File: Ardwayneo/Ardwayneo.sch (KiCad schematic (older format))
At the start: 13 parts, among them U1 24LC1025, U2 24LC1025, U3 ATMEGA328P-AU, Y1 Crystal 32MHz, Y2 Crystal 16MHz

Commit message: Completed all wiring
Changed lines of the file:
@@
 F16 "D7" B R 5875 6300 50
 F17 "D8" B R 5875 6450 50
+F18 "I2C" B R 5875 5275 50
 $EndSheet
 $Comp
@@
 Wire Wire Line
 	3900 5075 4125 5075
-Text Label 7250 3100 2    50   ~ 0
+Text Label 7450 3100 2    50   ~ 0
 MISO
-Wire Wire Line
-	7250 3100 7450 3100
 Text Label 3900 5300 2    50   ~ 0
 SCK
@@
 Text Label 3900 6625 2    50   ~ 0
 GND
-Text Label 7250 3000 2    50   ~ 0
+Text Label 7450 3000 2    50   ~ 0
 MOSI
-Wire Wire Line
-	7250 3000 7450 3000
-Text Label 7250 3200 2    50   ~ 0
+Text Label 7450 3200 2    50   ~ 0
 SCK
-Text Label 7250 3900 2    50   ~ 0
+Text Label 7450 3900 2    50   ~ 0
 RESET
 Wire Wire Line
@@
 Text Label 7250 2100 2    50   ~ 0
 D4
-Text Label 7250 2400 2    50   ~ 0
+Text Label 7450 2400 2    50   ~ 0
 D5
-Text Label 7250 2500 2    50   ~ 0
+Text Label 7450 2500 2    50   ~ 0
 D6
-Text Label 7250 2600 2    50   ~ 0
+Text Label 7450 2600 2    50   ~ 0
 D7
-Text Label 7250 2700 2    50   ~ 0
+Text Label 7450 2700 2    50   ~ 0
 D8
-Text Label 7250 3700 2    50   ~ 0
+Text Label 7450 3700 2    50   ~ 0
 SDA
-Text Label 7250 4000 2    50   ~ 0
+Text Label 7450 4000 2    50   ~ 0
 RX
-Text Label 7250 4100 2    50   ~ 0
+Text Label 7450 4100 2    50   ~ 0
 TX
-Text Label 7250 4200 2    50   ~ 0
+Text Label 7450 4200 2    50   ~ 0
 D2
 Wire Wire Line
@@
 Wire Wire Line
 	7450 2100 7250 2100
-Wire Wire Line
-	7250 2400 7450 2400
-Wire Wire Line
-	7450 2500 7250 2500
-Wire Wire Line
-	7250 2600 7450 2600
-Wire Wire Line
-	7450 2700 7250 2700
-Wire Wire Line
-	7250 3700 7450 3700
-Wire Wire Line
-	7450 4000 7250 4000
-Wire Wire Line
-	7250 4100 7450 4100
-Wire Wire Line
-	7450 4200 7250 4200
 $Comp
 L Device:Crystal Y1
@@
 Text Label 2300 3575 0    50   ~ 0
 SDA
-Text Label 7250 3800 2    50   ~ 0
+Text Label 7450 3800 2    50   ~ 0
 SCL
-Wire Wire Line
-	7250 3800 7450 3800
 Text Label 3650 3675 0    50   ~ 0
 SCL
@@
 Text Label 1500 3675 2    50   ~ 0
 ADDS2
-Text Label 7250 3300 2    50   ~ 0
+Text Label 7450 3300 2    50   ~ 0
 ADDS1
-Text Label 7250 3400 2    50   ~ 0
+Text Label 7450 3400 2    50   ~ 0
 ADDS2
-Wire Wire Line
-	7250 3300 7450 3300
-Wire Wire Line
-	7250 3400 7450 3400
 $Comp
 L power:GNDPWR #PWR0104
@@
 Connection ~ 8875 1350
 Wire Wire Line
-	8875 1350 8050 1350
+	8875 1350 8475 1350
 Text Label 8875 1200 0    50   ~ 0
 Vcc
@@
 Wire Wire Line
 	4575 2475 4575 2675
-Wire Wire Line
-	6275 3200 7450 3200
 $Comp
 L power:GNDPWR #PWR0106
@@
 Wire Wire Line
 	6650 4050 6650 3900
-Wire Wire Line
-	6650 3900 7450 3900
 Text Label 6500 4550 2    50   ~ 0
 Vcc
@@
 SDA
 NoConn ~ 2925 1625
+$Comp
+L power:PWR_FLAG #FLG0101
+U 1 1 6004FDBD
+P 8475 1175
+F 0 "#FLG0101" H 8475 1250 50  0001 C CNN
+F 1 "PWR_FLAG" H 8475 1348 50  0000 C CNN
+F 2 "" H 8475 1175 50  0001 C CNN
+F 3 "~" H 8475 1175 50  0001 C CNN
+	1    8475 1175
+	1    0    0    -1
+$EndComp
+Wire Wire Line
+	8475 1175 8475 1350
+Connection ~ 8475 1350
+Wire Wire Line
+	8475 1350 8050 1350
+Wire Wire Line
+	6650 3900 7450 3900
+Wire Wire Line
+	6275 3200 7450 3200
+Text Label 3900 5825 2    50   ~ 0
+RX
+Wire Wire Line
+	3900 5825 4125 5825
+Text Label 3900 6000 2    50   ~ 0
+TX
+Wire Wire Line
+	3900 6000 4125 6000
+Text Label 6100 5275 0    50   ~ 0
+I2C
+Wire Wire Line
+	6100 5275 5875 5275
 $EndSCHEMATC

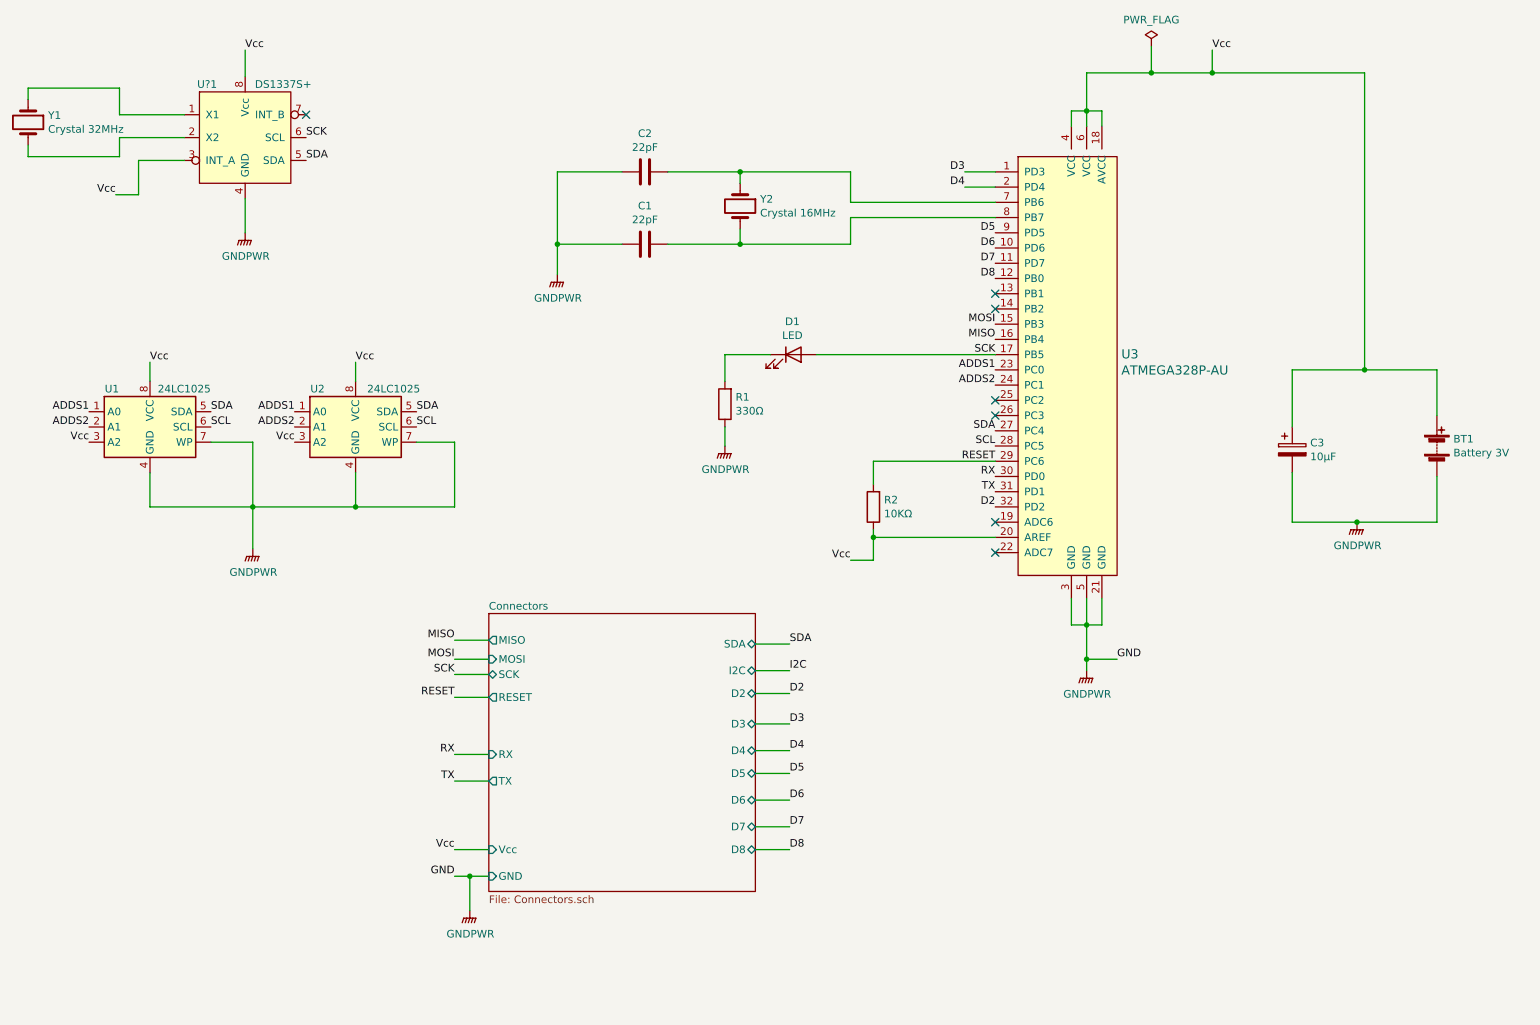
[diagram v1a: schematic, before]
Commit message: Added functional block descriptions
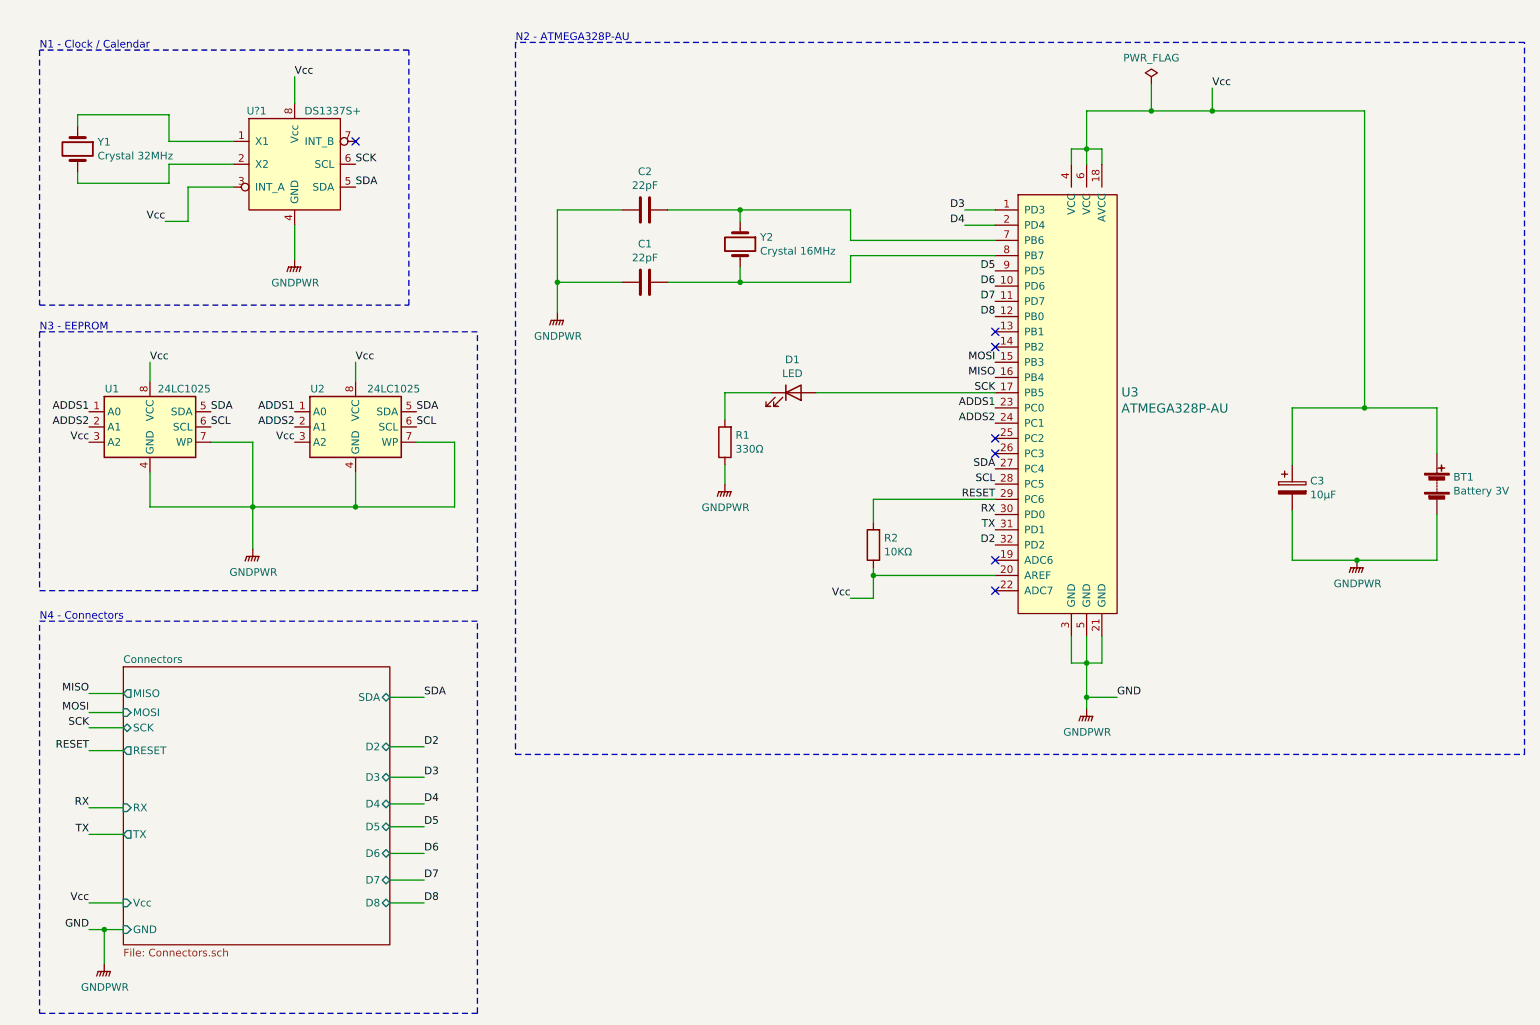
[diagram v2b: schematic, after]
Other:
- note added: "N1 - Clock / Calendar"
- note added: "N2 - ATMEGA328P-AU"
- note added: "N3 - EEPROM"
- note added: "N4 - Connectors"
- moved on the sheet: BT1, C1, C2, C3, D1, R1, R2, U3, U?1, Y1, Y2

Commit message: Fixed association for capacitor footprints
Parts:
- C1, C2, C3: footprint Connector_PinHeader_2.54mm:PinHeader_1x09_P2.54mm_Vertical -> Capacitor_SMD:C_0805_2012Metric_Pad1.18x1.45mm_HandSolder
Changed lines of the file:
@@
 F 0 "C1" V 5402 2725 50  0000 C CNN
 F 1 "22pF" V 5311 2725 50  0000 C CNN
-F 2 "Connector_PinHeader_2.54mm:PinHeader_1x09_P2.54mm_Vertical" H 5188 2575 50  0001 C CNN
+F 2 "Capacitor_SMD:C_0805_2012Metric_Pad1.18x1.45mm_HandSolder" H 5188 2575 50  0001 C CNN
 F 3 "~" H 5150 2725 50  0001 C CNN
 	1    5150 2725
@@
 F 0 "C2" V 4898 2250 50  0000 C CNN
 F 1 "22pF" V 4989 2250 50  0000 C CNN
-F 2 "Connector_PinHeader_2.54mm:PinHeader_1x09_P2.54mm_Vertical" H 5188 2100 50  0001 C CNN
+F 2 "Capacitor_SMD:C_0805_2012Metric_Pad1.18x1.45mm_HandSolder" H 5188 2100 50  0001 C CNN
 F 3 "~" H 5150 2250 50  0001 C CNN
 	1    5150 2250
@@
 F 0 "C3" H 9518 4121 50  0000 L CNN
 F 1 "10µF" H 9518 4030 50  0000 L CNN
-F 2 "Connector_PinHeader_2.54mm:PinHeader_1x09_P2.54mm_Vertical" H 9438 3925 50  0001 C CNN
+F 2 "Capacitor_SMD:C_0805_2012Metric_Pad1.18x1.45mm_HandSolder" H 9438 3925 50  0001 C CNN
 F 3 "~" H 9400 4075 50  0001 C CNN
 	1    9400 4075

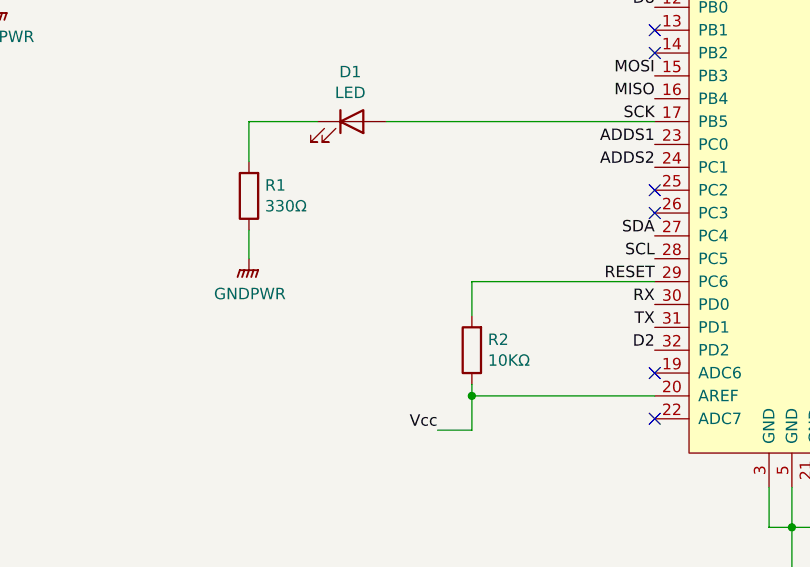
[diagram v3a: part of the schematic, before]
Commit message: Used 3rd pty autorouter, DRC checks out.
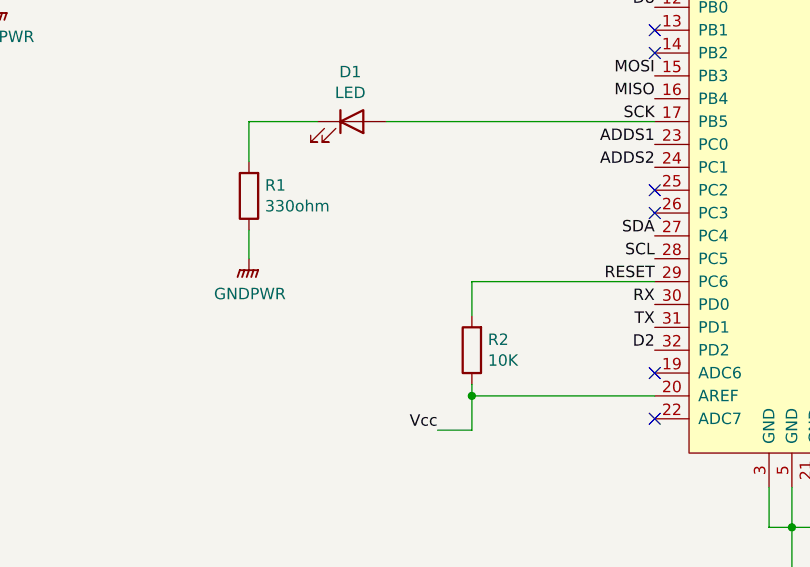
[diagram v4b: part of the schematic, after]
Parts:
- R1: value 330Ω -> 330ohm
- R2: value 10KΩ -> 10K
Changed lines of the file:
@@
 P 5675 3775
 F 0 "R1" H 5605 3729 50  0000 R CNN
-F 1 "330Ω" H 5605 3820 50  0000 R CNN
+F 1 "330ohm" H 5605 3820 50  0000 R CNN
 F 2 "Resistor_SMD:R_0805_2012Metric_Pad1.20x1.40mm_HandSolder" V 5605 3775 50  0001 C CNN
 F 3 "~" H 5675 3775 50  0001 C CNN
@@
 P 6650 4450
 F 0 "R2" H 6580 4404 50  0000 R CNN
-F 1 "10KΩ" H 6580 4495 50  0000 R CNN
+F 1 "10K" H 6580 4495 50  0000 R CNN
 F 2 "Resistor_SMD:R_0805_2012Metric_Pad1.20x1.40mm_HandSolder" V 6580 4450 50  0001 C CNN
 F 3 "~" H 6650 4450 50  0001 C CNN
